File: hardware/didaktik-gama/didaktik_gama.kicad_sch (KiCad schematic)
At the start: 176 parts, among them J1 Klávesnice, J2 MG, J4 Porty 8255, J5 Napájení 9–12V DC, J7 VGA DE-15 (RGB 15 kHz), J8 RGB z modulu ULA, SW1 RESET, T1 KSY72, T2 KSY72, T3 KC507, U1 UA880D (Z80), U10 4164, U11 4164, U12 4164, U13 4164, U14 4164, U15 4164, U16 4164, U17 2118, U18 2118, U19 2118, U2 27128 (16K EPROM), U20 2118, U21 2118, U22 2118, U23 2118, U24 2118, U25 74LS04, U26 74LS04, U27 74LS00, U28 74LS10, U29 74LS32, U3 8255 (MHB8255), U32 R-78E5.0-1.0 (spínaný, náhrad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, U37 74HCT244, U38 74HCT08, U39 Raspberry Pi Pico (USB host), U4 ULA, U40 74LVC245, U41 74LVC07, U5 74LS157, U6 74LS157, U7 74LS157, U8 74LS157, U9 4164, Y1 14MHz

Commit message: Add .TAP tape player from USB flash drive to Pico firmware and schematic
Pico GP14 drives MG_IN through a 10k/2k2 divider and 1u coupling cap.
Firmware: TinyUSB MSC host, minimal read-only FAT12/16/32 reader, TAP
pulse generator with standard ROM loader timing, alarm-driven output
from a pulse ring buffer; F1/F3 select file, F2 play/stop. Host tests
cover FAT images and decode the generated pulses back to bytes.

Co-Authored-By: Claude Opus 5.5 <noreply@anthropic.com>
Claude-Session: https://claude.ai/code/session_01LAVM7Gq9EYiUXiCEdy9ZRx
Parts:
- removed C8: 47p, Capacitor_THT:C_Disc_D5.0mm_W2.5mm_P5.00mm, symbol gama:C
- removed R41: 8k2, Resistor_THT:R_Axial_DIN0207_L6.3mm_D2.5mm_P10.16mm_Horizontal, symbol gama:R
- removed unit 4 of U25
- removed unit 7 of U25
- removed unit 6 of U25
- added C10: 100p, Capacitor_THT:C_Disc_D5.0mm_W2.5mm_P5.00mm, symbol gama:C
- added C85: 1u/16V, Capacitor_THT:CP_Radial_D5.0mm_P2.00mm, symbol gama:CP
- added R96: 10k, Resistor_THT:R_Axial_DIN0207_L6.3mm_D2.5mm_P10.16mm_Horizontal, symbol gama:R
- added R97: 2k2, Resistor_THT:R_Axial_DIN0207_L6.3mm_D2.5mm_P10.16mm_Horizontal, symbol gama:R
- added unit 2 of U25
- added U26: 74LS04, Package_DIP:DIP-14_W7.62mm, symbol gama:7404
- C8: renamed from C10; value 100p -> 47p
- R41: renamed from U25; value 74LS04 -> 8k2; footprint Package_DIP:DIP-14_W7.62mm -> Resistor_THT:R_Axial_DIN0207_L6.3mm_D2.5mm_P10.16mm_Horizontal; symbol gama:7404 -> gama:R
- renumbered U26 to U25
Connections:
- net +5V: now also R41.1, U26.14 (VCC)
- net BANK: now also U26.11, U26.2; no longer U25.11, U25.2
- net D6: now also R41.2
- net GND: now also C10.2, R97.2, U26.7 (GND)
- net IORQ_H: now also U25.8
- net MG_IN: now also C85.2
- net PC0: now also U26.1; no longer U25.1
- net RAS_D: now also C8.1
- net RESET: now also U25.12
- net WR_D: now also U25.4; no longer R41.4
- net WR_I: now also U25.3; no longer R41.3
- net ~{BANKSEL}: now also U26.10; no longer U25.10
- net ~{IORQ}: now also U25.9
- net ~{MREQ}: now also C10.1; no longer C8.1
- net ~{RESET}: now also U25.13
- net KBD_TAPE: now reaches U39.19 (GP14)
- net KBD_TAPE: now also R96.1
- new net TAPE_DIV: C85.1, R96.2, R97.1
- no-connect marks 34 -> 33
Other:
- note added: "• R96, R97, C85 (přehrávač kazet): GP14 Pica -> MG_IN, úroveň ~0,6 V jako výstup magnetofonu – Při nahrávání nemít připojený skutečný magnetofon (oba výstupy by se sčítaly); úroveň případně upravit R97"
- moved on the sheet: C8, U25D, U25F, U25G

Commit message: Add sound: YM2149/AY on 128K ports, LM386 amplifier and line out
Main board: YM2149F (AY-3-8910 pinout) decoded at FFFD/BFFD via 74HCT11
(A15, A14, A1, IORQ, WR, /M1), 1.75 MHz clock from CPU clock via
74HCT74, resistor mix of AY A/B/C and the beeper, volume pot, LM386 on
VIN to a speaker header and a 3.5 mm line out. Sheet enlarged to A0.
CPLD module: dedicated BEEP output on pin 35, J2/J8 extended to 10 pins.

Co-Authored-By: Claude Opus 5.5 <noreply@anthropic.com>
Claude-Session: https://claude.ai/code/session_01LAVM7Gq9EYiUXiCEdy9ZRx
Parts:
- removed J8: RGB z modulu ULA, Connector_PinHeader_2.54mm:PinHeader_1x08_P2.54mm_Vertical, symbol gama:CONN_8
- removed R76: 680, Resistor_THT:R_Axial_DIN0207_L6.3mm_D2.5mm_P10.16mm_Horizontal, symbol gama:R
- removed R90, R96: 10k, Resistor_THT:R_Axial_DIN0207_L6.3mm_D2.5mm_P10.16mm_Horizontal, symbol gama:R
- removed U12, U15, U9: 4164, Package_DIP:DIP-16_W7.62mm, symbol gama:4164
- removed unit 7 of U25
- removed unit 1 of U26
- removed unit 4 of U28
- added C30, C31, C39, C83, C91, C94, C95: 100n, Capacitor_THT:C_Disc_D5.0mm_W2.5mm_P5.00mm, symbol gama:C
- added C86, C87, C92: 10u/16V, Capacitor_THT:CP_Radial_D6.3mm_P2.50mm, symbol gama:CP
- added C88: 220u/16V, Capacitor_THT:CP_Radial_D6.3mm_P2.50mm, symbol gama:CP
- added C89: 47n, Capacitor_THT:C_Disc_D5.0mm_W2.5mm_P5.00mm, symbol gama:C
- added C90: 100u/25V, Capacitor_THT:CP_Radial_D6.3mm_P2.50mm, symbol gama:CP
- added J10: Linkový výstup (jack 3,5 mm), Connector_Audio:Jack_3.5mm_CUI_SJ1-3523N_Horizontal, symbol gama:CONN_3
- added J5: Napájení 9–12V DC, Connector_BarrelJack:BarrelJack_Horizontal, symbol gama:CONN_2
- added J8: RGB + zvuk z modulu ULA, Connector_PinHeader_2.54mm:PinHeader_1x10_P2.54mm_Vertical, symbol gama:CONN_10
- added J9: Reproduktor 8 ohm, Connector_PinHeader_2.54mm:PinHeader_1x02_P2.54mm_Vertical, symbol gama:CONN_2
- added R100, R108, R99: 1k, Resistor_THT:R_Axial_DIN0207_L6.3mm_D2.5mm_P10.16mm_Horizontal, symbol gama:R
- added R101, R102, R103: 4k7, Resistor_THT:R_Axial_DIN0207_L6.3mm_D2.5mm_P10.16mm_Horizontal, symbol gama:R
- added R104, R84: 10k, Resistor_THT:R_Axial_DIN0207_L6.3mm_D2.5mm_P10.16mm_Horizontal, symbol gama:R
- added R105: 100k, Resistor_THT:R_Axial_DIN0207_L6.3mm_D2.5mm_P10.16mm_Horizontal, symbol gama:R
- added R106, R97: 2k2, Resistor_THT:R_Axial_DIN0207_L6.3mm_D2.5mm_P10.16mm_Horizontal, symbol gama:R
- added R107: 10R, Resistor_THT:R_Axial_DIN0207_L6.3mm_D2.5mm_P10.16mm_Horizontal, symbol gama:R
- added R109: 47k, Resistor_THT:R_Axial_DIN0207_L6.3mm_D2.5mm_P10.16mm_Horizontal, symbol gama:R
- added R20: 470, Resistor_THT:R_Axial_DIN0207_L6.3mm_D2.5mm_P10.16mm_Horizontal, symbol gama:R
- added R42: 8k2, Resistor_THT:R_Axial_DIN0207_L6.3mm_D2.5mm_P10.16mm_Horizontal, symbol gama:R
- added RV1: 10k log (hlasitost), Potentiometer_THT:Potentiometer_Alps_RK09K_Single_Vertical, symbol gama:POT
- added U22: 2118, Package_DIP:DIP-16_W7.62mm, symbol gama:2118
- added unit 2 of U26
- added unit 3 of U29
- added U42: YM2149F (nebo AY-3-8910), Package_DIP:DIP-40_W15.24mm, symbol gama:YM2149
- added U43: 74HCT11, Package_DIP:DIP-14_W7.62mm, symbol gama:74HCT11
- added U44: 74HCT74, Package_DIP:DIP-14_W7.62mm, symbol gama:74HCT74
- added U45: LM386N-1, Package_DIP:DIP-8_W7.62mm, symbol gama:LM386
- C93: renamed from R20; value 470 -> 100n; footprint Resistor_THT:R_Axial_DIN0207_L6.3mm_D2.5mm_P10.16mm_Horizontal -> Capacitor_THT:C_Disc_D5.0mm_W2.5mm_P5.00mm; symbol gama:R -> gama:C
- R76: renamed from R77; value 1k5 -> 680
- R77: renamed from R78; value 680 -> 1k5
- R78: renamed from R79; value 1k5 -> 680
- R79: renamed from R80; value 680 -> 1k5
- R80: renamed from R81; value 1k5 -> 680
- R81: renamed from R82; value 75 -> 1k5
- R83: renamed from R84; value 10k -> 75
- R95: renamed from C83; value 100n -> 10k; footprint Capacitor_THT:C_Disc_D5.0mm_W2.5mm_P5.00mm -> Resistor_THT:R_Axial_DIN0207_L6.3mm_D2.5mm_P10.16mm_Horizontal; symbol gama:C -> gama:R
- R96: renamed from R97; value 2k2 -> 10k
- R98: renamed from U22; value 2118 -> 1k; footprint Package_DIP:DIP-16_W7.62mm -> Resistor_THT:R_Axial_DIN0207_L6.3mm_D2.5mm_P10.16mm_Horizontal; symbol gama:2118 -> gama:R
- U12: renamed from U29; value 74LS32 -> 4164; footprint Package_DIP:DIP-14_W7.62mm -> Package_DIP:DIP-16_W7.62mm; symbol gama:7432 -> gama:4164
- U15: renamed from J5; value Napájení 9–12V DC -> 4164; footprint Connector_BarrelJack:BarrelJack_Horizontal -> Package_DIP:DIP-16_W7.62mm; symbol gama:CONN_2 -> gama:4164
- U25: renamed from C30; value 100n -> 74LS04; footprint Capacitor_THT:C_Disc_D5.0mm_W2.5mm_P5.00mm -> Package_DIP:DIP-14_W7.62mm; symbol gama:C -> gama:7404
- U26: renamed from C31; value 100n -> 74LS04; footprint Capacitor_THT:C_Disc_D5.0mm_W2.5mm_P5.00mm -> Package_DIP:DIP-14_W7.62mm; symbol gama:C -> gama:7404
- U28: renamed from C39; value 100n -> 74LS10; footprint Capacitor_THT:C_Disc_D5.0mm_W2.5mm_P5.00mm -> Package_DIP:DIP-14_W7.62mm; symbol gama:C -> gama:7410
- U9: renamed from R42; value 8k2 -> 4164; footprint Resistor_THT:R_Axial_DIN0207_L6.3mm_D2.5mm_P10.16mm_Horizontal -> Package_DIP:DIP-16_W7.62mm; symbol gama:R -> gama:4164
- renumbered R83 to R82, R91 to R90, R92 to R91, R93 to R92, R94 to R93, R95 to R94
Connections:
- net +3V3_KBD: now also C83.1
- net +5V: now also C93.1, U12.8 (VCC), U15.8 (VCC), U25.14 (VCC), U28.14 (VCC), U9.8 (VCC), C30.1, C31.1, C39.1, C94.1, C95.1, J8.7, R42.1, U22.8 (VCC), U22.9 (VCC), U42.25 (A8), U42.26 (SEL), U42.28 (BC2), U42.40 (VCC), U43.14 (VCC), U44.1 (~{1CLR}), U44.10 (~{2PRE}), U44.13 (~{2CLR}), U44.14 (VCC), U44.4 (~{1PRE}); no longer R98.8 (VCC), R98.9 (VCC), U25.1, U26.1, U28.1, U9.1
- net A1: now also U26.3
- net A14: now also U43.5 (2C)
- net A15: now also U43.10 (3B), U43.4 (2B)
- net BANK: now also U26.2
- net CLK: now also U44.3 (1CLK)
- net D0: now also U9.14 (Q), U9.2 (D), U42.37 (DA0)
- net D1: now also R20.1, U42.36 (DA1); no longer C93.1
- net D2: now also U42.35 (DA2)
- net D3: now also U12.14 (Q), U12.2 (D), U42.34 (DA3)
- net D4: now also U42.33 (DA4)
- net D5: now also U42.32 (DA5)
- net D6: now also U15.14 (Q), U15.2 (D), U42.31 (DA6)
- net D7: now also R42.2, U42.30 (DA7); no longer U9.2
- net DACB_B: now also R81.1; no longer R80.1
- net DACB_G: now also R79.1; no longer R78.1
- net DACB_R: now also R77.1; no longer R76.1
- net DAC_B: now also R80.1; no longer R79.1
- net DAC_G: now also R78.1; no longer R77.1
- net DAC_R: now also R76.1
- net GND: now also C93.2, R98.2, U12.16 (GND), U15.16 (GND), U25.7 (GND), U28.7 (GND), U9.16 (GND), C30.2, C31.2, C39.2, C83.2, C87.2, C89.2, C90.2, C91.2, C94.2, C95.2, J10.3, J5.2, J8.10, J8.8, J9.2, R100.2, R105.2, R106.2, R109.2, R84.2, R97.2, R99.2, RV1.3, U22.16 (GND), U42.1 (GND), U42.24 (~{A9}), U43.7 (GND), U44.11 (2CLK), U44.12 (2D), U44.7 (GND), U45.2 (-IN), U45.4 (GND); no longer R83.2, R95.2, R96.2, R98.16 (GND), U15.2, U25.2, U26.2, U28.2
- net IORQ_H: now also U43.1 (1A)
- net KBD_KB1: now also R90.2
- net KBD_KB2: now also R91.2; no longer R90.2
- net KBD_KB3: now also R92.2; no longer R91.2
- net KBD_KB4: now also R93.2; no longer R92.2
- net KBD_KB5: now also R94.2; no longer R93.2
- net KBD_RST: now also R95.2; no longer R94.2
- net KBD_TAPE: now also R96.1
- net MUX2: now also U29.8; no longer U12.8
- net PC0: now also U26.1
- net RA0: now also U12.5 (A0), U15.5 (A0), U9.5 (A0)
- net RA1: now also U12.7 (A1), U15.7 (A1), U9.7 (A1)
- net RA2: now also U12.6 (A2), U15.6 (A2), U9.6 (A2)
- net RA3: now also U12.12 (A3), U15.12 (A3), U9.12 (A3)
- net RA4: now also U12.11 (A4), U15.11 (A4), U9.11 (A4)
- net RA5: now also U12.10 (A5), U15.10 (A5), U9.10 (A5)
- net RA6: now also U12.13 (A6), U15.13 (A6), U9.13 (A6)
- net RA7: now also U12.9 (A7), U15.9 (A7), U9.9 (A7)
- net RAS_D: now also U29.9; no longer U12.9
- net RGB_B: now also J8.3
- net RGB_G: now also J8.2
- net RGB_I: now also J8.4
- net RGB_R: now also J8.1, R84.1; no longer R83.1
- net TAPE_DIV: now also R96.2, R97.1; no longer R96.1
- net VA0: now also U22.5 (A0); no longer R98.5 (A0)
- net VA1: now also U22.11 (A4); no longer R98.11 (A4)
- net VA2: now also U22.7 (A1); no longer R98.7 (A1)
- net VA3: now also U22.13 (A6); no longer R98.13 (A6)
- net VA4: now also U22.12 (A3); no longer R98.12 (A3)
- net VA5: now also U22.10 (A5); no longer R98.10 (A5)
- net VA6: now also U22.6 (A2); no longer R98.6 (A2)
- net VD1: now also R20.2; no longer C93.2
- net VD5: now also U22.14 (Q), U22.2 (D); no longer R98.14 (Q), R98.2 (D)
- net VGA_B: now also R81.2; no longer R79.2
- net VGA_G: now also R79.2; no longer R77.2
- net VGA_HS: now also R82.2; no longer R81.2
- net VGA_HS_D: now also R82.1; no longer R81.1
- net VGA_R: now also R77.2
- net VGA_VS: now also R83.2; no longer R82.2
- net VGA_VS_D: now also R83.1; no longer R82.1
- net VIN: now also C90.1, C91.1, U45.6 (VS)
- net VIN_RAW: now also J5.1; no longer U15.1
- net WR_I: now also U43.11 (3C)
- net ~{CAS64}: now also U12.15 (~{CAS}), U15.15 (~{CAS}), U9.15 (~{CAS})
- net ~{M1}: now also U43.2 (1B)
- net ~{RAS64}: now also U12.4 (~{RAS}), U15.4 (~{RAS}), U9.4 (~{RAS})
- net ~{RESET}: now also U42.23 (~{RESET})
- net ~{RGB_CSYNC}: now also J8.5
- net ~{RGB_VSYNC}: now also J8.6
- net ~{SEL64}: now also U29.10; no longer U12.10
- net ~{VCAS}: now also U22.15 (~{CAS}); no longer R98.15 (~{CAS})
- net ~{VRAS}: now also U22.4 (~{RAS}); no longer R98.4 (~{RAS})
- net ~{VWE}: now also U22.3 (~{WE}); no longer R98.3 (~{WE})
- net ~{WE64}: now also U12.3 (~{WE}), U15.3 (~{WE}), U9.3 (~{WE})
- net AY_A: now reaches R98.1
- net AY_A: now also R101.1, U42.4 (ANALOG_A)
- new net A1_N: U26.4, U43.13 (1C)
- new net AMP_BYP: C87.1, U45.7 (BYPASS)
- new net AMP_IN: RV1.2 (W), U45.3 (+IN)
- new net AMP_OUT: C88.1, R107.1, U45.5 (OUT)
- new net AY_B: R102.1, R99.1, U42.3 (ANALOG_B)
- new net AY_BC1: U42.29 (BC1), U43.6 (2Y)
- new net AY_BDIR: U42.27 (BDIR), U43.8 (3Y)
- new net AY_C: R100.1, R103.1, U42.38 (ANALOG_C)
- new net AY_CLK: U42.22 (CLOCK), U44.5 (1Q)
- new net AY_CLK_N: U44.2 (1D), U44.6 (~{1Q})
- new net AY_IOX: U43.12 (1Y), U43.3 (2A), U43.9 (3A)
- new net BEEP: J8.9, R104.1, R105.1
- new net LINE_AC: C92.2, R108.1
- new net LINE_OUT: J10.1, J10.2, R108.2, R109.1
- new net MIX: C86.1, C92.1, R101.2, R102.2, R103.2, R104.2, R106.1
- new net MIX_AC: C86.2, RV1.1
- new net SPK_OUT: C88.2, J9.1
- new net ZOBEL: C89.1, R107.2
- no-connect marks 33 -> 56
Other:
- note added: "ZVUK: YM2149/AY (porty FFFD/BFFD jako Spectrum 128K) + BEEP z modulu -> LM386 a linkový výstup"
- note added: "• U42 YM2149F: pinout AY-3-8910/YM2149 (DIP-40), pin 26 (SEL) na +5V = hodiny bez dělení – Ověřit s datasheetem; u AY-3-8910 je pin 26 TEST2 – nezapojovat (přerušit spoj na +5V)"
- note added: "• U43 dekódování AY: FFFD = výběr registru, BFFD = data (A15, A14, A1, IORQ, WR, /M1) – Shodné s portem Spectra 128K; Gama 8255 (A7=0, A1=1) ani ULA (A0=0) nekolidují"
- note added: "• Zvuk – mix a LM386: BEEP 10k + AY 3x 4k7 do 2k2, hlasitost 10k, LM386 z VIN 9 V – Poměr hlasitosti beeperu a AY podle sluchu (R104); LS1 a D9/D10 z původního zapojení neosazovat, reproduktor na J9"
- moved on the sheet: R76, R77, R78, R79, R80, R81, R82, R83, R90, R91, R92, R93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

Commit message: Add CPLD ULA firmware (Verilog) with simulation testbench
Original ULA implementation for the XC95144XL module: 448x312 video
timing, page-mode 2118 fetch, RAS-only refresh, CPU access with early
write, clock-stretch contention, port FE, /INT, /ROMCS, digital RGBI
and sync outputs, BEEP. Icarus testbench models the 2118, the address
multiplexer and a Z80 bus; renders a test frame and checks timing,
memory access, ports and DRAM refresh.

Also: YM2149 /SEL left open per datasheet (internal pull-up), 74HCT244
pin labels per datasheet, note on 330R isolation resistors.

Co-Authored-By: Claude Opus 5.5 <noreply@anthropic.com>
Claude-Session: https://claude.ai/code/session_01LAVM7Gq9EYiUXiCEdy9ZRx
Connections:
- net +5V: no longer U42.26 (SEL)
- no-connect marks 56 -> 57
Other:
- note added: "• R27–R33 (330R): oddělení multiplexeru od adresy DRAM – S modulem CPLD (3,3 V) zvážit 470R – omezí proud do výstupů CPLD, když ULA přebíjí multiplexer"
- note added: "• U42 YM2149F: pinout ověřen katalogovým listem Yamaha YM2149 (1992) – Pin 26 /SEL nezapojen – vnitřní pull-up = hodiny bez dělení (1,75 MHz jako AY); totéž funguje s AY-3-8910"
- note removed: "• U42 YM2149F: pinout AY-3-8910/YM2149 (DIP-40), pin 26 (SEL) na +5V = hodiny bez dělení – Ověřit s datasheetem; u AY-3-8910 je pin 26 TEST2 – nezapojovat (přerušit spoj na +5V)"

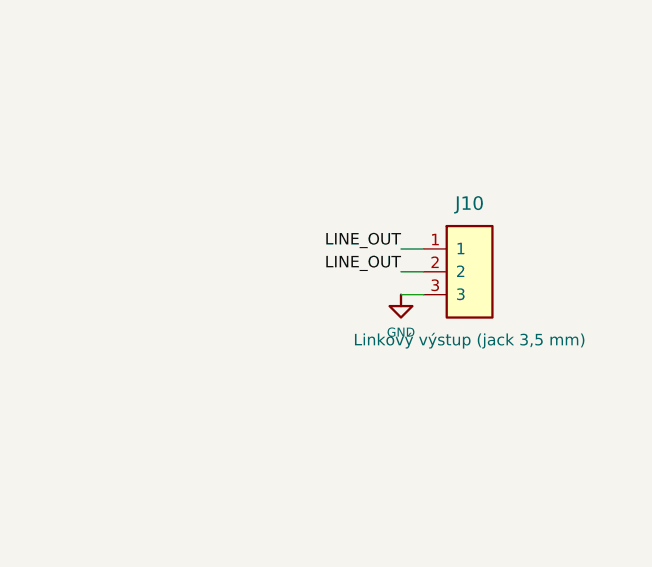
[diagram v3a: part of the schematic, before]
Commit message: Add main board PCB (placed, nets assigned, 4-layer with GND/+5V planes)
gen_pcb.py builds didaktik_gama.kicad_pcb from netlist.py via pcbnew:
300x225 mm outline, M3 mounting holes, block-wise placement with
decoupling caps next to each IC, edge connectors on the top edge,
inner GND and +5V zones. DRC: no courtyard/outline errors; signal
routing left for KiCad/Freerouting. Custom Pico footprint, audio jack
symbol uses T/R/S pads.

Co-Authored-By: Claude Opus 5.5 <noreply@anthropic.com>
Claude-Session: https://claude.ai/code/session_01LAVM7Gq9EYiUXiCEdy9ZRx
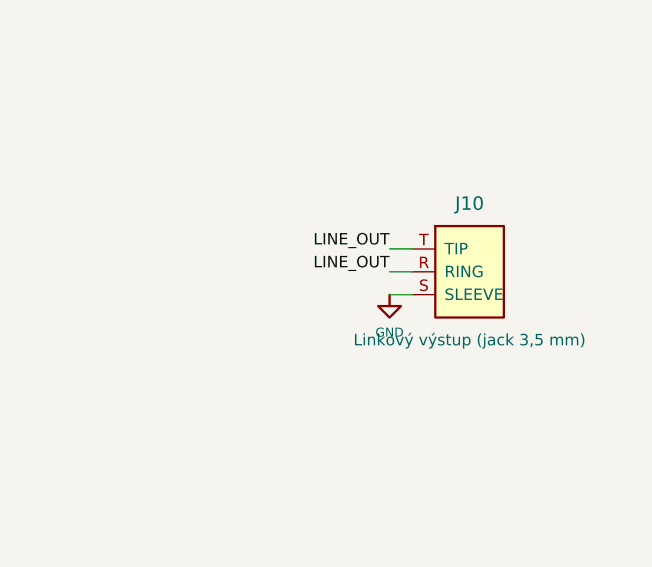
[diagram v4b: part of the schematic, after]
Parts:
- J10: symbol gama:CONN_3 -> gama:JACK3
- U39: footprint (none) -> gama:RaspberryPi_Pico_THT
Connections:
- net GND: now also J10.S (SLEEVE); no longer J10.3
- net LINE_OUT: now also J10.R (RING), J10.T (TIP); no longer J10.1, J10.2
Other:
- moved on the sheet: J10
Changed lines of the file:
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@@
   (wire
     (pts
-      (xy 1125.22 147.32)
-      (xy 1122.68 147.32))
+      (xy 1123.95 147.32)
+      (xy 1121.41 147.32))
     (stroke
       (width 0)
@@
   (wire
     (pts
-      (xy 1125.22 149.86)
-      (xy 1122.68 149.86))
+      (xy 1123.95 149.86)
+      (xy 1121.41 149.86))
     (stroke
       (width 0)
@@
   (wire
     (pts
-      (xy 1125.22 152.40)
-      (xy 1122.68 152.40))
+      (xy 1123.95 152.40)
+      (xy 1121.41 152.40))
     (stroke
       (width 0)
@@
 )
   (label "LINE_OUT"
-    (at 1122.68 147.32 180)
+    (at 1121.41 147.32 180)
     (fields_autoplaced yes)
     (effects
@@
 )
   (label "LINE_OUT"
-    (at 1122.68 149.86 180)
+    (at 1121.41 149.86 180)
     (fields_autoplaced yes)
     (effects
@@
       (effects
         (font (size 1.27 1.27))))
-    (property "Footprint" ""
+    (property "Footprint" "gama:RaspberryPi_Pico_THT"
       (at 558.80 469.90 0)
       (effects
@@
         (path "/749bded9-dac2-5d4c-8e6d-156d036e5f62" (reference "J9") (unit 1)))))
   (symbol
-    (lib_id "gama:CONN_3")
+    (lib_id "gama:JACK3")
     (at 1130.30 149.86 0)
     (unit 1)
@@
       (effects
         (font (size 1.27 1.27)) hide))
-    (pin "1"
+    (pin "T"
 )
-    (pin "2"
+    (pin "R"
 )
-    (pin "3"
+    (pin "S"
 )
     (instances
@@
   (symbol
     (lib_id "power:GND")
-    (at 1122.68 152.40 0)
+    (at 1121.41 152.40 0)
     (unit 1)
     (exclude_from_sim no)
@@
     (dnp no)
     (property "Reference" "#PWR095"
-      (at 1122.68 152.40 0)
+      (at 1121.41 152.40 0)
       (effects
         (font (size 1.27 1.27)) hide))
     (property "Value" "GND"
-      (at 1122.68 156.60 0)
+      (at 1121.41 156.60 0)
       (effects
         (font (size 1.0 1.0))))
     (property "Footprint" ""
-      (at 1122.68 152.40 0)
+      (at 1121.41 152.40 0)
       (effects
         (font (size 1.27 1.27)) hide))
     (property "Datasheet" ""
-      (at 1122.68 152.40 0)
+      (at 1121.41 152.40 0)
       (effects
         (font (size 1.27 1.27)) hide))
